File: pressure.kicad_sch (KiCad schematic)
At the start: 12 parts, among them U4 TLV9101IDBVR

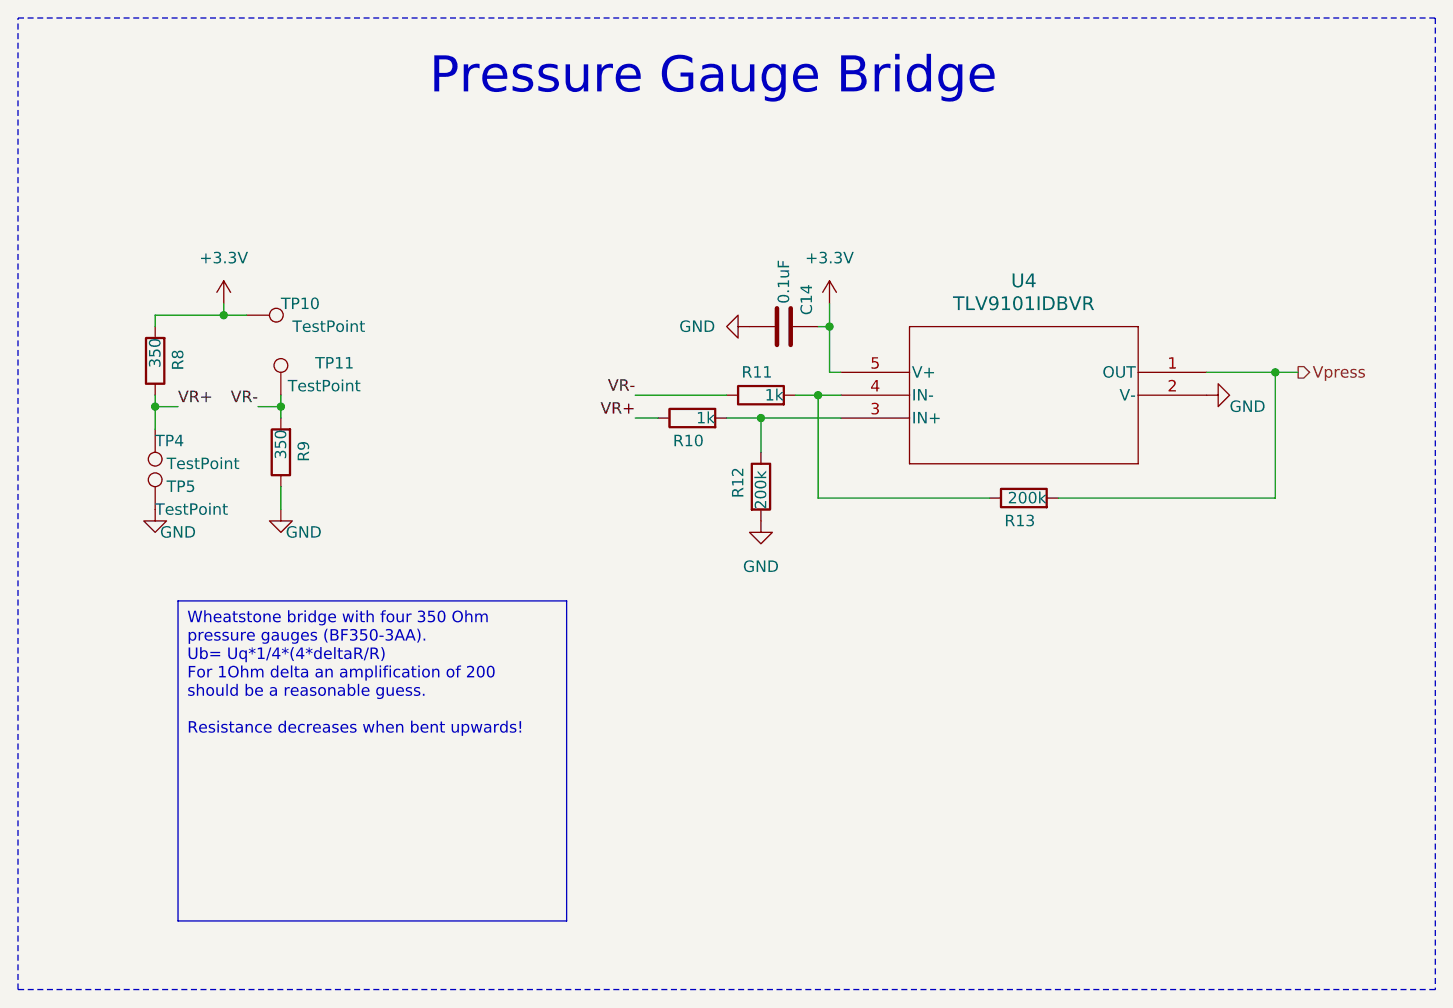
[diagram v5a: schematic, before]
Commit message: reannotate components and move some designators
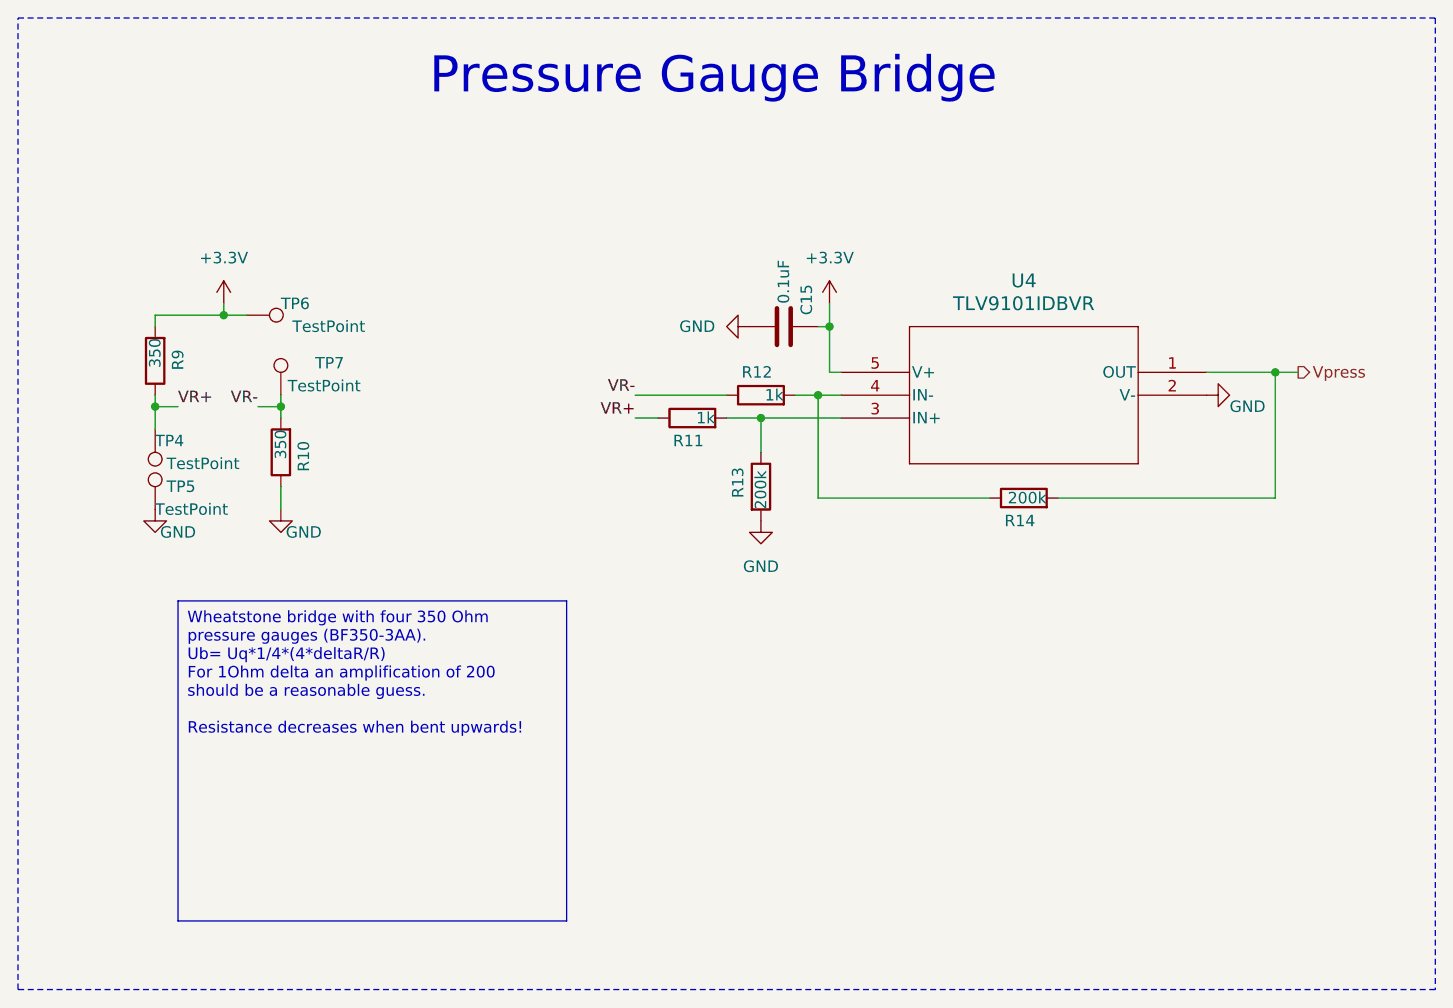
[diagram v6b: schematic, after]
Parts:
- renumbered C14 to C15, R9 to R10, R10 to R11, R11 to R12, R12 to R13, R13 to R14, R8 to R9, TP10 to TP6, TP11 to TP7
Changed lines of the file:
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@@
 		(on_board yes)
 		(dnp no)
-		(property "Reference" "TP11"
+		(property "Reference" "TP7"
 			(at 58.42 58.674 0)
 			(effects
@@
 			(project "bierdeckel"
 				(path "/a4ffe097-37ef-4e19-a91a-ae57f4a5aad1/67cff1c4-a4ae-4e77-90c9-75aa7da1f628"
-					(reference "TP11")
+					(reference "TP7")
 					(unit 1)
 				)
@@
 		(dnp no)
 		(fields_autoplaced yes)
-		(property "Reference" "#PWR052"
+		(property "Reference" "#PWR050"
 			(at 107.95 82.55 0)
 			(effects
@@
 			(project "bierdeckel"
 				(path "/a4ffe097-37ef-4e19-a91a-ae57f4a5aad1/67cff1c4-a4ae-4e77-90c9-75aa7da1f628"
-					(reference "#PWR052")
+					(reference "#PWR050")
 					(unit 1)
 				)
@@
 		(on_board yes)
 		(dnp no)
-		(property "Reference" "TP10"
+		(property "Reference" "TP6"
 			(at 54.61 52.07 90)
 			(effects
@@
 			(project "bierdeckel"
 				(path "/a4ffe097-37ef-4e19-a91a-ae57f4a5aad1/67cff1c4-a4ae-4e77-90c9-75aa7da1f628"
-					(reference "TP10")
+					(reference "TP6")
 					(unit 1)
 				)
@@
 		(dnp no)
 		(fields_autoplaced yes)
-		(property "Reference" "#PWR048"
+		(property "Reference" "#PWR047"
 			(at 48.26 55.88 0)
 			(effects
@@
 			(project "bierdeckel"
 				(path "/a4ffe097-37ef-4e19-a91a-ae57f4a5aad1/67cff1c4-a4ae-4e77-90c9-75aa7da1f628"
-					(reference "#PWR048")
+					(reference "#PWR047")
 					(unit 1)
 				)
@@
 		(on_board yes)
 		(dnp no)
-		(property "Reference" "R10"
+		(property "Reference" "R11"
 			(at 101.6 67.31 90)
 			(effects
@@
 			(project "bierdeckel"
 				(path "/a4ffe097-37ef-4e19-a91a-ae57f4a5aad1/67cff1c4-a4ae-4e77-90c9-75aa7da1f628"
-					(reference "R10")
+					(reference "R11")
 					(unit 1)
 				)
@@
 		(on_board yes)
 		(dnp no)
-		(property "Reference" "R8"
+		(property "Reference" "R9"
 			(at 43.18 57.15 90)
 			(effects
@@
 			(project "bierdeckel"
 				(path "/a4ffe097-37ef-4e19-a91a-ae57f4a5aad1/67cff1c4-a4ae-4e77-90c9-75aa7da1f628"
-					(reference "R8")
+					(reference "R9")
 					(unit 1)
 				)
@@
 		(on_board yes)
 		(dnp no)
-		(property "Reference" "R9"
+		(property "Reference" "R10"
 			(at 57.15 67.31 90)
 			(effects
@@
 			(project "bierdeckel"
 				(path "/a4ffe097-37ef-4e19-a91a-ae57f4a5aad1/67cff1c4-a4ae-4e77-90c9-75aa7da1f628"
-					(reference "R9")
+					(reference "R10")
 					(unit 1)
 				)
@@
 		(on_board yes)
 		(dnp no)
-		(property "Reference" "R12"
+		(property "Reference" "R13"
 			(at 105.41 73.66 90)
 			(effects
@@
 			(project "bierdeckel"
 				(path "/a4ffe097-37ef-4e19-a91a-ae57f4a5aad1/67cff1c4-a4ae-4e77-90c9-75aa7da1f628"
-					(reference "R12")
+					(reference "R13")
 					(unit 1)
 				)
@@
 		(on_board yes)
 		(dnp no)
-		(property "Reference" "R11"
+		(property "Reference" "R12"
 			(at 109.22 59.69 90)
 			(effects
@@
 			(project "bierdeckel"
 				(path "/a4ffe097-37ef-4e19-a91a-ae57f4a5aad1/67cff1c4-a4ae-4e77-90c9-75aa7da1f628"
-					(reference "R11")
+					(reference "R12")
 					(unit 1)
 				)
@@
 		(on_board yes)
 		(dnp no)
-		(property "Reference" "#PWR053"
+		(property "Reference" "#PWR051"
 			(at 115.57 55.88 0)
 			(effects
@@
 			(project "bierdeckel"
 				(path "/a4ffe097-37ef-4e19-a91a-ae57f4a5aad1/67cff1c4-a4ae-4e77-90c9-75aa7da1f628"
-					(reference "#PWR053")
+					(reference "#PWR051")
 					(unit 1)
 				)
@@
 		(on_board yes)
 		(dnp no)
-		(property "Reference" "#PWR054"
+		(property "Reference" "#PWR052"
 			(at 163.83 62.23 0)
 			(effects
@@
 			(project "bierdeckel"
 				(path "/a4ffe097-37ef-4e19-a91a-ae57f4a5aad1/67cff1c4-a4ae-4e77-90c9-75aa7da1f628"
-					(reference "#PWR054")
+					(reference "#PWR052")
 					(unit 1)
 				)
@@
 		(on_board yes)
 		(dnp no)
-		(property "Reference" "C14"
+		(property "Reference" "C15"
 			(at 113.03 53.34 0)
 			(effects
@@
 			(project "bierdeckel"
 				(path "/a4ffe097-37ef-4e19-a91a-ae57f4a5aad1/67cff1c4-a4ae-4e77-90c9-75aa7da1f628"
-					(reference "C14")
+					(reference "C15")
 					(unit 1)
 				)
@@
 		(dnp no)
 		(fields_autoplaced yes)
-		(property "Reference" "#PWR051"
+		(property "Reference" "#PWR049"
 			(at 100.33 54.61 0)
 			(effects
@@
 			(project "bierdeckel"
 				(path "/a4ffe097-37ef-4e19-a91a-ae57f4a5aad1/67cff1c4-a4ae-4e77-90c9-75aa7da1f628"
-					(reference "#PWR051")
+					(reference "#PWR049")
 					(unit 1)
 				)
@@
 		(on_board yes)
 		(dnp no)
-		(property "Reference" "#PWR049"
+		(property "Reference" "#PWR046"
 			(at 40.64 81.28 0)
 			(effects
@@
 			(project "bierdeckel"
 				(path "/a4ffe097-37ef-4e19-a91a-ae57f4a5aad1/67cff1c4-a4ae-4e77-90c9-75aa7da1f628"
-					(reference "#PWR049")
+					(reference "#PWR046")
 					(unit 1)
 				)
@@
 		(on_board yes)
 		(dnp no)
-		(property "Reference" "#PWR050"
+		(property "Reference" "#PWR048"
 			(at 54.61 81.28 0)
 			(effects
@@
 			(project "bierdeckel"
 				(path "/a4ffe097-37ef-4e19-a91a-ae57f4a5aad1/67cff1c4-a4ae-4e77-90c9-75aa7da1f628"
-					(reference "#PWR050")
+					(reference "#PWR048")
 					(unit 1)
 				)
@@
 		(on_board yes)
 		(dnp no)
-		(property "Reference" "R13"
+		(property "Reference" "R14"
 			(at 138.43 76.2 90)
 			(effects
@@
 			(project "bierdeckel"
 				(path "/a4ffe097-37ef-4e19-a91a-ae57f4a5aad1/67cff1c4-a4ae-4e77-90c9-75aa7da1f628"
-					(reference "R13")
-					(unit 1)
-				)
+					(reference "R14")
+					(unit 1)
+				)

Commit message: update design
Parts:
- added R15, R16: 1k, Resistor_SMD:R_0805_2012Metric, symbol Device:R
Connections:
- net GND: no longer R10.1, TP5.1
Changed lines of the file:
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@@
 	(text_box "Wheatstone bridge with four 350 Ohm pressure gauges (BF350-3AA).\nUb= Uq*1/4*(4*deltaR/R)\nFor 1Ohm delta an amplification of 200 should be a reasonable guess.\n\nResistance decreases when bent upwards!"
 		(exclude_from_sim no)
-		(at 43.18 85.09 0)
+		(at 66.04 86.36 0)
 		(size 43.18 35.56)
 		(stroke
@@
 	)
 	(symbol
+		(lib_id "Device:R")
+		(at 54.61 80.01 180)
+		(unit 1)
+		(exclude_from_sim no)
+		(in_bom yes)
+		(on_board yes)
+		(dnp no)
+		(property "Reference" "R16"
+			(at 52.07 78.74 90)
+			(effects
+				(font
+					(size 1.27 1.27)
+				)
+				(justify left)
+			)
+		)
+		(property "Value" "1k"
+			(at 54.61 77.47 90)
+			(effects
+				(font
+					(size 1.27 1.27)
+				)
+				(justify left)
+			)
+		)
+		(property "Footprint" "Resistor_SMD:R_0805_2012Metric"
+			(at 56.388 80.01 90)
+			(effects
+				(font
+					(size 1.27 1.27)
+				)
+				(hide yes)
+			)
+		)
+		(property "Datasheet" "~"
+			(at 54.61 80.01 0)
+			(effects
+				(font
+					(size 1.27 1.27)
+				)
+				(hide yes)
+			)
+		)
+		(property "Description" "Resistor"
+			(at 54.61 80.01 0)
+			(effects
+				(font
+					(size 1.27 1.27)
+				)
+				(hide yes)
+			)
+		)
+		(property "mpn" "CR0805-FX-1002ELF "
+			(at 54.61 80.01 0)
+			(effects
+				(font
+					(size 1.27 1.27)
+				)
+				(hide yes)
+			)
+		)
+		(pin "1"
+		)
+		(pin "2"
+		)
+		(instances
+			(project "bierdeckel"
+				(path "/a4ffe097-37ef-4e19-a91a-ae57f4a5aad1/67cff1c4-a4ae-4e77-90c9-75aa7da1f628"
+					(reference "R16")
+					(unit 1)
+				)
+			)
+		)
+	)
+	(symbol
 		(lib_id "Connector:TestPoint")
 		(at 40.64 66.04 180)
@@
 	)
 	(symbol
+		(lib_id "Device:R")
+		(at 40.64 80.01 180)
+		(unit 1)
+		(exclude_from_sim no)
+		(in_bom yes)
+		(on_board yes)
+		(dnp no)
+		(property "Reference" "R15"
+			(at 38.1 78.74 90)
+			(effects
+				(font
+					(size 1.27 1.27)
+				)
+				(justify left)
+			)
+		)
+		(property "Value" "1k"
+			(at 40.64 77.47 90)
+			(effects
+				(font
+					(size 1.27 1.27)
+				)
+				(justify left)
+			)
+		)
+		(property "Footprint" "Resistor_SMD:R_0805_2012Metric"
+			(at 42.418 80.01 90)
+			(effects
+				(font
+					(size 1.27 1.27)
+				)
+				(hide yes)
+			)
+		)
+		(property "Datasheet" "~"
+			(at 40.64 80.01 0)
+			(effects
+				(font
+					(size 1.27 1.27)
+				)
+				(hide yes)
+			)
+		)
+		(property "Description" "Resistor"
+			(at 40.64 80.01 0)
+			(effects
+				(font
+					(size 1.27 1.27)
+				)
+				(hide yes)
+			)
+		)
+		(property "mpn" "CR0805-FX-1002ELF "
+			(at 40.64 80.01 0)
+			(effects
+				(font
+					(size 1.27 1.27)
+				)
+				(hide yes)
+			)
+		)
+		(pin "1"
+		)
+		(pin "2"
+		)
+		(instances
+			(project "bierdeckel"
+				(path "/a4ffe097-37ef-4e19-a91a-ae57f4a5aad1/67cff1c4-a4ae-4e77-90c9-75aa7da1f628"
+					(reference "R15")
+					(unit 1)
+				)
+			)
+		)
+	)
+	(symbol
 		(lib_id "power:GND")
-		(at 40.64 74.93 0)
+		(at 40.64 85.09 0)
 		(mirror y)
 		(unit 1)
@@
 		(dnp no)
 		(property "Reference" "#PWR046"
-			(at 40.64 81.28 0)
+			(at 40.64 91.44 0)
 			(effects
 				(font
@@
 		)
 		(property "Value" "GND"
-			(at 43.18 77.47 0)
+			(at 43.18 87.63 0)
 			(effects
 				(font
@@
 		)
 		(property "Footprint" ""
-			(at 40.64 74.93 0)
+			(at 40.64 85.09 0)
 			(effects
 				(font
@@
 		)
 		(property "Datasheet" ""
-			(at 40.64 74.93 0)
+			(at 40.64 85.09 0)
 			(effects
 				(font
@@
 		)
 		(property "Description" "Power symbol creates a global label with name \"GND\" , ground"
-			(at 40.64 74.93 0)
+			(at 40.64 85.09 0)
 			(effects
 				(font
@@
 	(symbol
 		(lib_id "power:GND")
-		(at 54.61 74.93 0)
+		(at 54.61 85.09 0)
 		(mirror y)
 		(unit 1)
@@
 		(dnp no)
 		(property "Reference" "#PWR048"
-			(at 54.61 81.28 0)
+			(at 54.61 91.44 0)
 			(effects
 				(font
@@
 		)
 		(property "Value" "GND"
-			(at 57.15 77.47 0)
+			(at 57.15 87.63 0)
 			(effects
 				(font
@@
 		)
 		(property "Footprint" ""
-			(at 54.61 74.93 0)
+			(at 54.61 85.09 0)
 			(effects
 				(font
@@
 		)
 		(property "Datasheet" ""
-			(at 54.61 74.93 0)
+			(at 54.61 85.09 0)
 			(effects
 				(font
@@
 		)
 		(property "Description" "Power symbol creates a global label with name \"GND\" , ground"
-			(at 54.61 74.93 0)
-			(effects
-				(font
+			(at 54.61 85.09 0)
+			(effects
+				(font

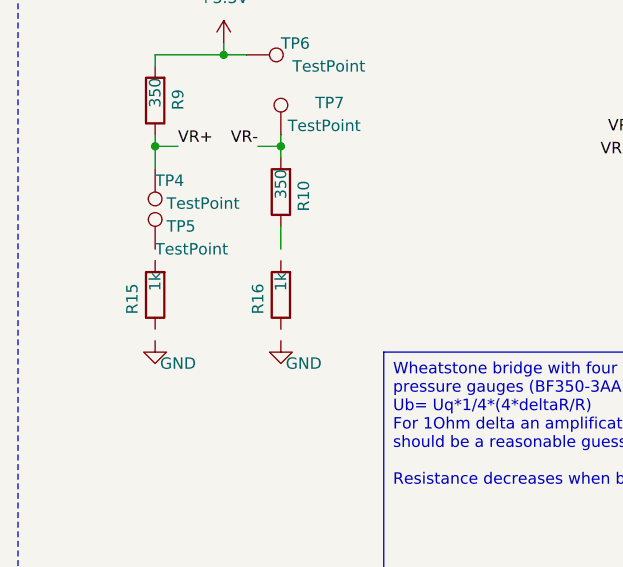
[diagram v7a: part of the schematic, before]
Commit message: fix ERC and DRC
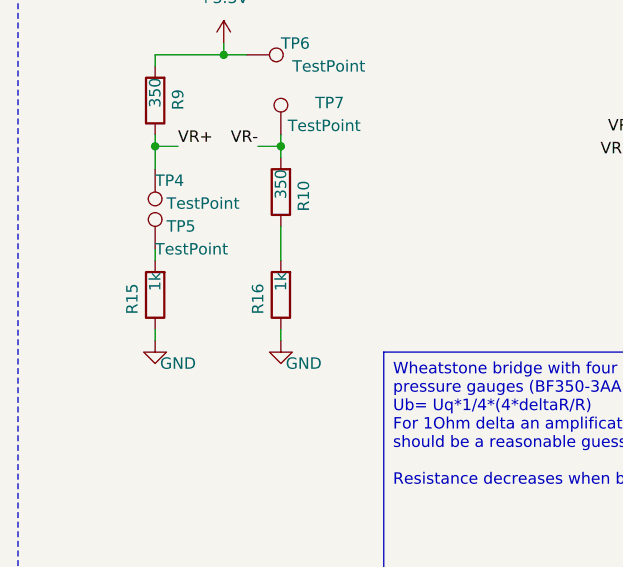
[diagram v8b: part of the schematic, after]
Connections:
- net GND: now also R15.1, R16.1
- net at R10.1: now also R16.2
- net at TP5.1: now also R15.2
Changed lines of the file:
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@@
+	(wire
+		(pts
+			(xy 54.61 85.09) (xy 54.61 83.82)
+		)
+		(stroke
+			(width 0)
+			(type default)
+		)
+	)
 	(wire
 		(pts
@@
 	(wire
 		(pts
-			(xy 54.61 72.39) (xy 54.61 74.93)
+			(xy 54.61 72.39) (xy 54.61 76.2)
 		)
 		(stroke
@@
 	(wire
 		(pts
+			(xy 40.64 85.09) (xy 40.64 83.82)
+		)
+		(stroke
+			(width 0)
+			(type default)
+		)
+	)
+	(wire
+		(pts
 			(xy 111.76 62.23) (xy 114.3 62.23)
 		)
@@
 		(pts
 			(xy 104.14 64.77) (xy 107.95 64.77)
+		)
+		(stroke
+			(width 0)
+			(type default)
+		)
+	)
+	(wire
+		(pts
+			(xy 40.64 76.2) (xy 40.64 74.93)
 		)
 		(stroke
@@
 	(label "VR+"
 		(at 93.98 64.77 180)
-		(fields_autoplaced yes)
 		(effects
 			(font
@@
 	(label "VR-"
 		(at 52.07 63.5 180)
-		(fields_autoplaced yes)
 		(effects
 			(font
@@
 	(label "VR-"
 		(at 93.98 62.23 180)
-		(fields_autoplaced yes)
 		(effects
 			(font
@@
 	(label "VR+"
 		(at 43.18 63.5 0)
-		(fields_autoplaced yes)
 		(effects
 			(font
@@
 		(shape output)
 		(at 167.64 59.69 0)
-		(fields_autoplaced yes)
-		(effects
-			(font
+		(effects
+			(font
